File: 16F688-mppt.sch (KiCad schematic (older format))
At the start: 45 parts, among them Q1 BUK9511-55A127, Q2 BUK9511-55A127, Q3 2N2222A, Q4 2N2222A, Q5 2N2907A, SW1 Write OP-AMP DIFF, U1 7805, U2 LM358N, U3 PIC16F688

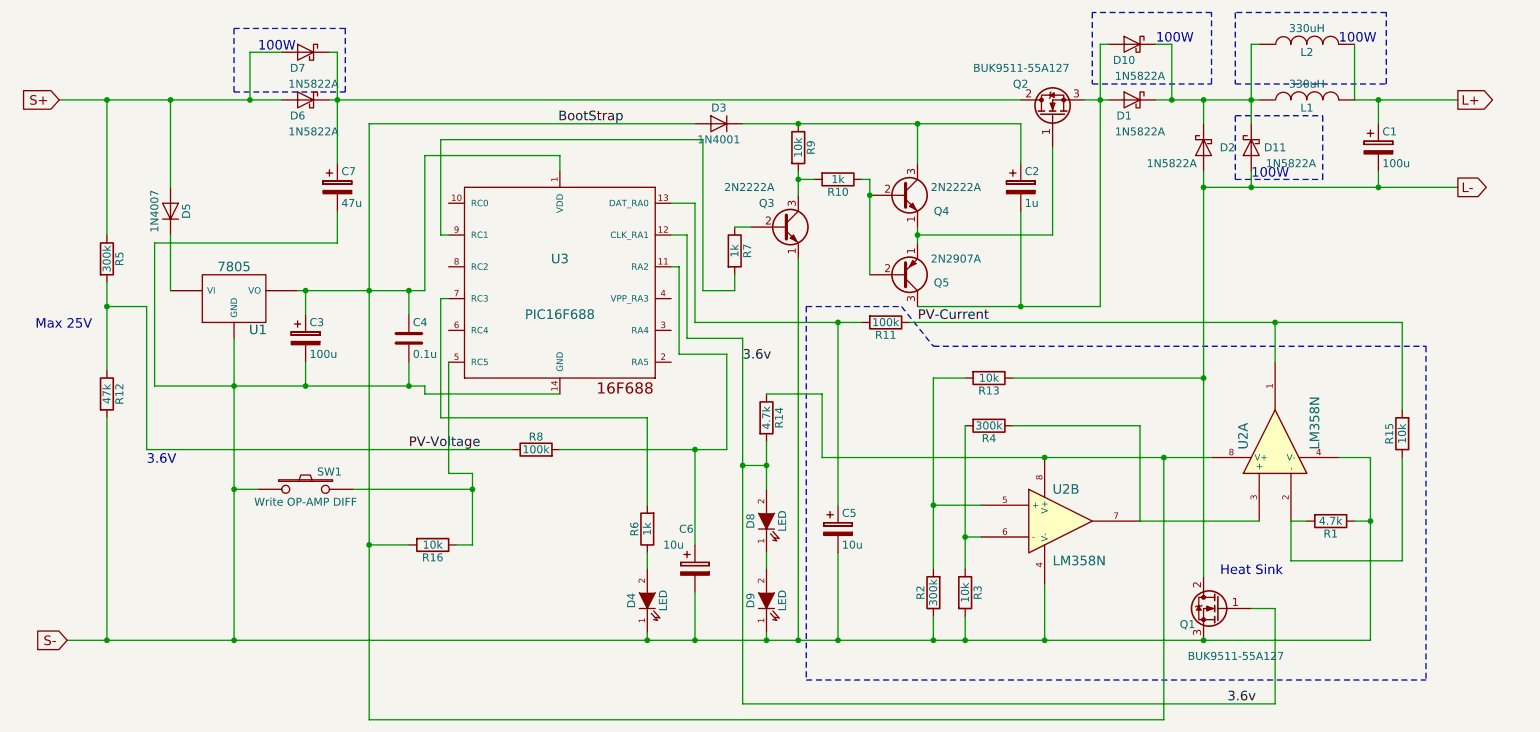
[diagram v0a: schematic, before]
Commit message: update schematic and code.
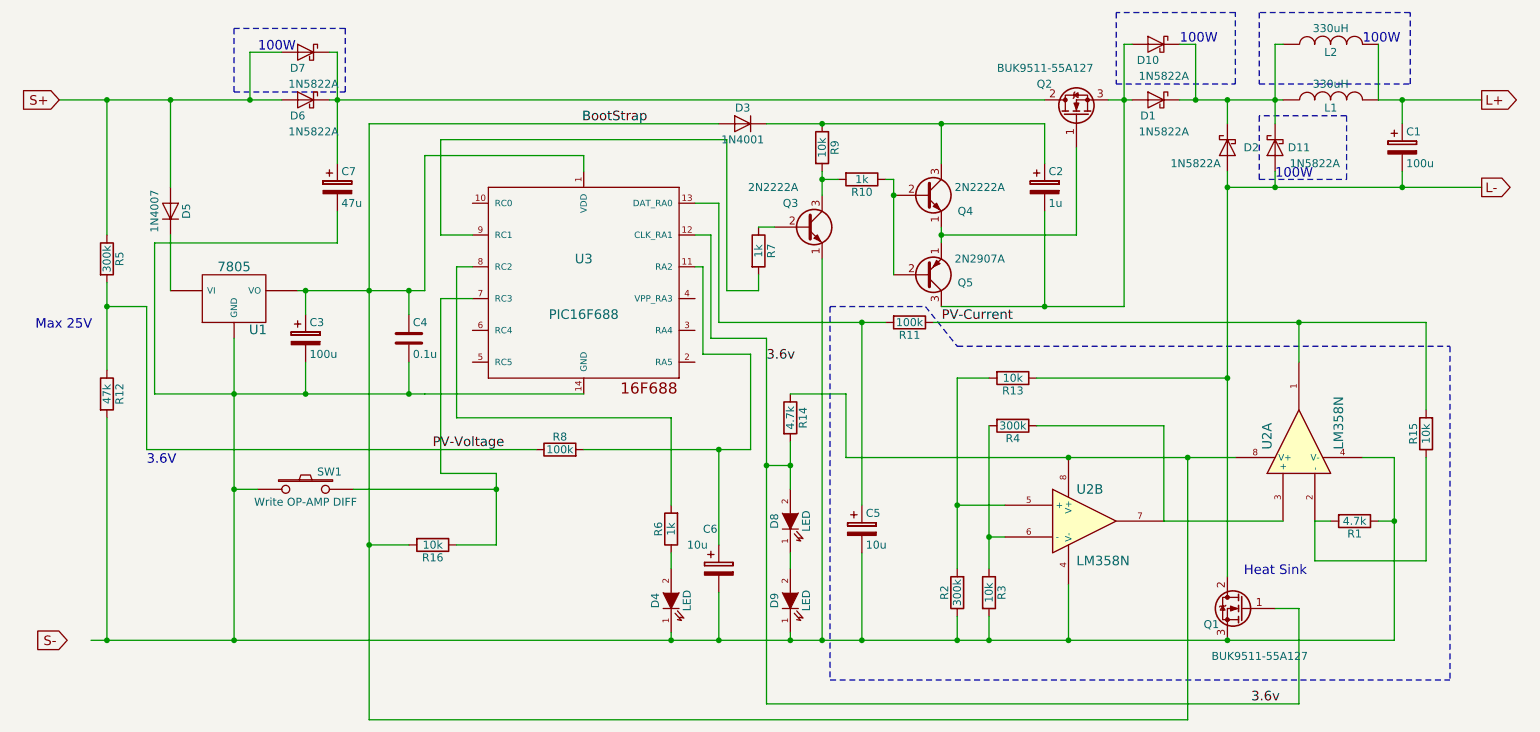
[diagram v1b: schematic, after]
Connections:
- net S-: no longer C3.2, C4.2, C5.2, C6.2, C7.2, D4.1 (K), D9.1 (K), Q1.3 (S), Q3.1 (E), R1.1, R12.2, R2.1, R3.2, SW1.1, U1.GND, U2.4 (V-), U2.4 (V-), U3.14 (GND)
- net at R6.2: now also U3.8 (RC2); no longer U3.7 (RC3)
- net at R16.1, SW1.2: now also U3.7 (RC3); no longer U3.5 (RC5)
- new net: C3.2, C4.2, C5.2, C6.2, C7.2, D4.1 (K), D9.1 (K), Q1.3 (S), Q3.1 (E), R1.1, R12.2, R2.1, R3.2, SW1.1, U1.GND, U2.4 (V-), U2.4 (V-), U3.14 (GND)
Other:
- moved on the sheet: C1, C2, C5, C6, D1, D10, D11, D2, D3, D4, D8, D9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

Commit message: More circuit simple.
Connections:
- net at R6.2: now also U3.6 (RC4); no longer U3.8 (RC2)
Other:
- moved on the sheet: D4, R6
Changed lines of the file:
@@
 Title "Simple MPPT with 16F688 v1"
 Date "2018-06-12"
-Rev "1.1"
+Rev "1.2"
 Comp ""
 Comment1 ""
@@
 L R R6
 U 1 1 55C3BCB8
-P 5050 4900
-F 0 "R6" V 5130 4900 50  0000 C CNN
-F 1 "1k" V 5050 4900 50  0000 C CNN
-F 2 "" V 4980 4900 30  0000 C CNN
-F 3 "" H 5050 4900 30  0000 C CNN
-	1    5050 4900
+P 4600 4800
+F 0 "R6" V 4680 4800 50  0000 C CNN
+F 1 "1k" V 4600 4800 50  0000 C CNN
+F 2 "" V 4530 4800 30  0000 C CNN
+F 3 "" H 4600 4800 30  0000 C CNN
+	1    4600 4800
 	-1   0    0    1
 $EndComp
@@
 L LED-RESCUE-12f675-mppt D4
 U 1 1 55C3BFD1
-P 5050 5350
-F 0 "D4" H 5050 5450 50  0000 C CNN
-F 1 "LED" H 5050 5250 50  0000 C CNN
-F 2 "" H 5050 5350 60  0000 C CNN
-F 3 "" H 5050 5350 60  0000 C CNN
-	1    5050 5350
+P 4600 5250
+F 0 "D4" H 4600 5350 50  0000 C CNN
+F 1 "LED" H 4600 5150 50  0000 C CNN
+F 2 "" H 4600 5250 60  0000 C CNN
+F 3 "" H 4600 5250 60  0000 C CNN
+	1    4600 5250
 	0    -1   -1   0
 $EndComp
@@
 	2750 4050 3400 4050
 Wire Wire Line
-	3400 4050 3500 4050
+	3400 4050 4500 4050
 Wire Wire Line
 	2300 3700 2300 4050
@@
 Connection ~ 1500 3500
 Wire Wire Line
-	5050 5600 5050 5550
-Connection ~ 5050 5600
-Wire Wire Line
-	5050 5150 5050 5050
+	4600 5600 4600 5450
+Connection ~ 4600 5600
+Wire Wire Line
+	4600 5050 4600 4950
 Wire Wire Line
 	1900 3050 1900 3400
@@
 	3150 6100 8300 6100
 Wire Wire Line
-	8300 6100 8300 4450
-Wire Wire Line
-	5050 4200 5050 4750
+	8300 4450 8300 6100
+Wire Wire Line
+	4600 4200 4600 4650
 Wire Wire Line
 	5350 5600 5350 5300
@@
 	5800 5600 5350 5600
 Wire Wire Line
-	5350 5600 5050 5600
-Wire Wire Line
-	5050 5600 2300 5600
+	5350 5600 4600 5600
+Wire Wire Line
+	4600 5600 2300 5600
 Wire Wire Line
 	2300 5600 1500 5600
@@
 Connection ~ 3150 5000
 Wire Wire Line
-	3950 5000 3950 4650
-Wire Wire Line
-	3950 4650 3950 4550
-Wire Wire Line
-	3700 5000 3950 5000
+	3950 4550 3950 4650
+Wire Wire Line
+	3950 4650 3950 5000
+Wire Wire Line
+	3950 5000 3700 5000
 Connection ~ 3950 4650
 Wire Wire Line
@@
 	4500 2550 4500 2650
 Wire Wire Line
-	3500 4050 3500 4050
-Wire Wire Line
-	3500 4050 4500 4050
-Wire Wire Line
 	3600 2450 5400 2450
 Wire Wire Line
 	5400 2450 5400 3400
 Wire Wire Line
-	3700 4200 5050 4200
+	3700 4200 4600 4200
 Wire Wire Line
 	5350 3600 5350 2850
@@
 	9300 2300 8750 2300
 Wire Wire Line
-	3700 3250 3800 3250
-Wire Wire Line
-	3700 3250 3700 4200
-Wire Wire Line
 	3600 4550 3600 3450
 Wire Wire Line
 	3600 3450 3800 3450
+Wire Wire Line
+	3800 3650 3700 3650
+Wire Wire Line
+	3700 3650 3700 4200
 $EndSCHEMATC

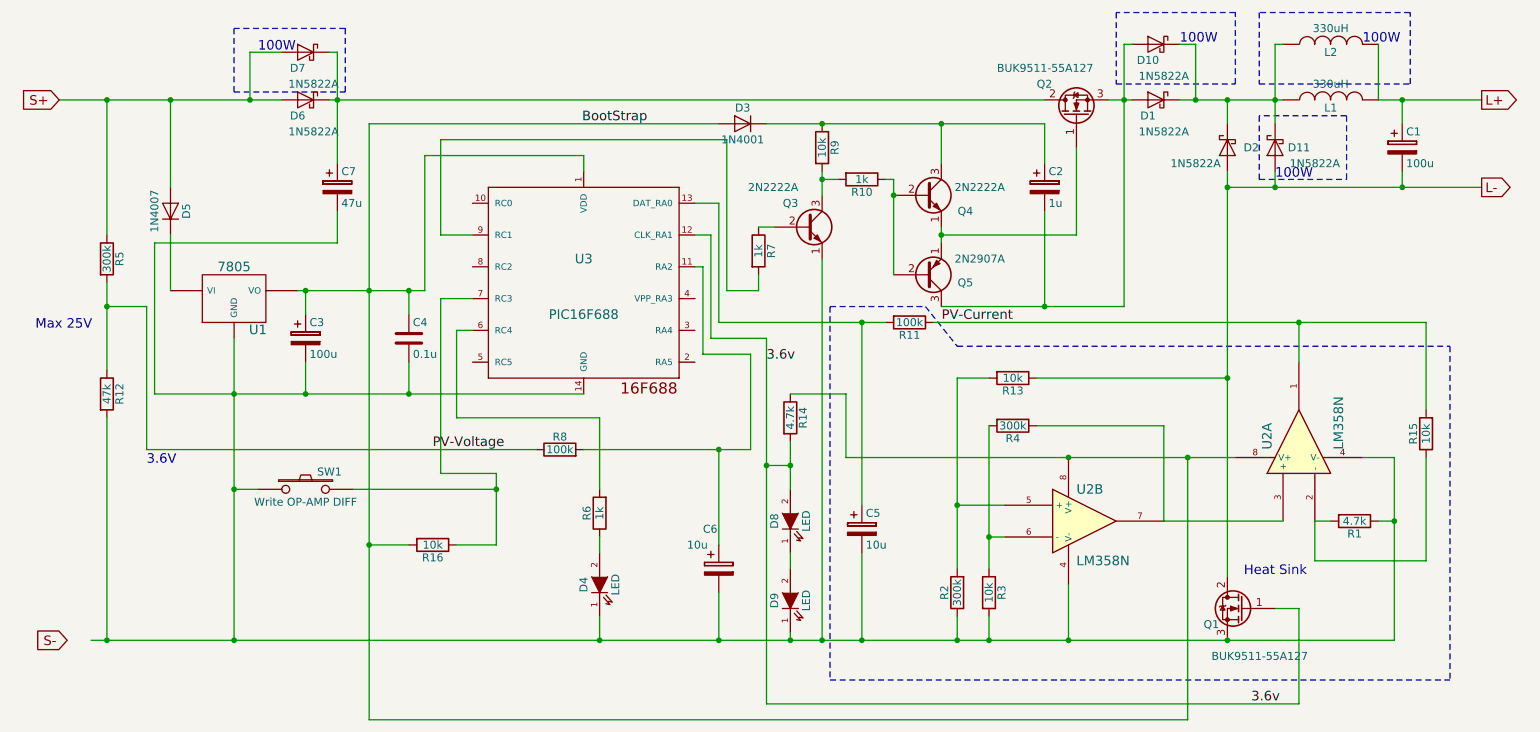
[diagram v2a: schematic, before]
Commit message: make word size and delay 300ms on op-amp calibration.
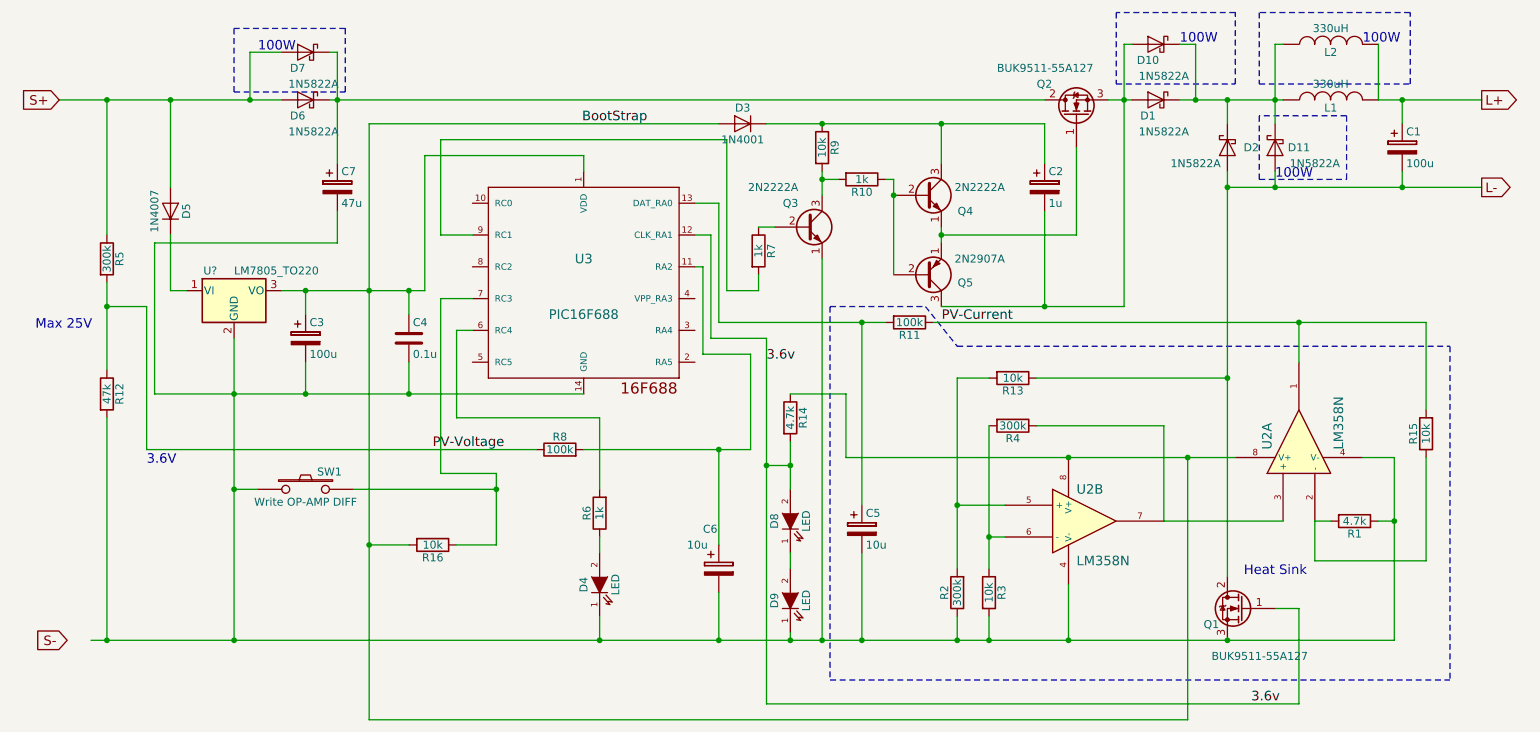
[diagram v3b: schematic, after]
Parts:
- removed U1: 7805, symbol 7805
- added U?: LM7805_TO220, TO_SOT_Packages_THT:TO-220_Vertical, symbol LM7805_TO220
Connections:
- net BootStrap: now also U?.3 (VO)
- net at C3.2, C4.2, C5.2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: now also U?.2 (GND)
- net at D5.1 (K): now also U?.1 (VI)
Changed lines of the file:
@@
 $EndDescr
-$Comp
-L 7805 U1
-U 1 1 55C337A7
-P 2300 3450
-F 0 "U1" H 2450 3254 60  0000 C CNN
-F 1 "7805" H 2300 3650 60  0000 C CNN
-F 2 "" H 2300 3450 60  0000 C CNN
-F 3 "" H 2300 3450 60  0000 C CNN
-	1    2300 3450
-	1    0    0    -1
-$EndComp
 $Comp
 L Q_NMOS_GDS Q1
@@
 100W
 Wire Wire Line
-	1800 4050 2300 4050
-Wire Wire Line
-	2300 4050 2750 4050
-Wire Wire Line
-	2750 4050 3400 4050
-Wire Wire Line
-	3400 4050 4500 4050
-Wire Wire Line
-	2300 3700 2300 4050
-Wire Wire Line
-	2300 4050 2300 4650
-Wire Wire Line
-	2300 4650 2300 5600
+	1800 4050 4500 4050
+Wire Wire Line
+	2300 3700 2300 5600
 Connection ~ 2300 4050
 Wire Wire Line
-	2700 3400 2750 3400
-Wire Wire Line
-	2750 3400 3150 3400
-Wire Wire Line
-	3150 3400 3400 3400
-Wire Wire Line
-	3400 3400 3500 3400
+	2600 3400 3500 3400
 Wire Wire Line
 	7550 5600 7550 5250
 Wire Wire Line
-	3150 2350 3150 3400
-Wire Wire Line
-	3150 3400 3150 5000
-Wire Wire Line
-	3150 5000 3150 6100
+	3150 2350 3150 6100
 Connection ~ 3150 3400
 Wire Wire Line
@@
 	7150 4950 7050 4950
 Wire Wire Line
-	7050 4250 7050 4950
-Wire Wire Line
-	7050 4950 7050 5150
+	7050 4250 7050 5150
 Connection ~ 7050 4950
 Wire Wire Line
 	6850 4750 7150 4750
 Wire Wire Line
-	8550 2650 8550 2750
-Wire Wire Line
-	8550 2750 8550 3950
-Wire Wire Line
-	8550 3950 8550 5200
-Wire Wire Line
-	8550 2750 8850 2750
-Wire Wire Line
-	8850 2750 9650 2750
-Wire Wire Line
-	9650 2750 10150 2750
-Wire Wire Line
-	8250 2200 8350 2200
-Wire Wire Line
-	8350 2200 8550 2200
-Wire Wire Line
-	8550 2200 8850 2200
-Wire Wire Line
-	8850 2200 8900 2200
+	8550 2650 8550 5200
+Wire Wire Line
+	8550 2750 10150 2750
+Wire Wire Line
+	8250 2200 8900 2200
 Wire Wire Line
 	8550 2200 8550 2350
 Connection ~ 8550 2200
 Wire Wire Line
-	9500 2200 9650 2200
-Wire Wire Line
-	9650 2200 10150 2200
+	9500 2200 10150 2200
 Wire Wire Line
 	9650 2200 9650 2350
 Wire Wire Line
-	7800 2200 7900 2200
-Wire Wire Line
-	7900 2200 7950 2200
-Wire Wire Line
-	6750 3000 6750 3050
-Wire Wire Line
-	6750 3050 6750 3100
+	7800 2200 7950 2200
+Wire Wire Line
+	6750 3000 6750 3100
 Wire Wire Line
 	6750 3050 7600 3050
@@
 Connection ~ 6750 3050
 Wire Wire Line
-	7900 3500 7400 3500
-Wire Wire Line
-	7400 3500 6750 3500
-Wire Wire Line
-	7900 1850 7900 2200
-Wire Wire Line
-	7900 2200 7900 3500
+	7900 3500 6750 3500
+Wire Wire Line
+	7900 1850 7900 3500
 Connection ~ 7900 2200
 Wire Wire Line
-	6450 2700 6450 2800
-Wire Wire Line
-	6450 2800 6450 3300
+	6450 2700 6450 3300
 Wire Wire Line
 	7400 2900 7400 3500
@@
 Connection ~ 6000 5600
 Wire Wire Line
-	6000 2650 6000 2700
-Wire Wire Line
-	6000 2700 6000 2800
+	6000 2650 6000 2800
 Wire Wire Line
 	5400 3400 5600 3400
@@
 	5600 3000 5700 3000
 Wire Wire Line
-	5650 2350 6000 2350
-Wire Wire Line
-	6000 2350 6750 2350
-Wire Wire Line
-	6750 2350 7400 2350
+	5650 2350 7400 2350
 Wire Wire Line
 	6750 2350 6750 2600
@@
 	1500 3050 1500 2200
 Wire Wire Line
-	1500 3350 1500 3500
-Wire Wire Line
-	1500 3500 1500 3900
+	1500 3350 1500 3900
 Wire Wire Line
 	1750 3500 1500 3500
@@
 	6050 5850 9950 5850
 Wire Wire Line
-	5350 3600 6250 3600
-Wire Wire Line
-	6250 3600 6400 3600
+	5350 3600 6400 3600
 Wire Wire Line
 	1500 4200 1500 5600
 Connection ~ 1500 5600
 Wire Wire Line
-	6850 3950 6850 4750
-Wire Wire Line
-	6850 4750 6850 5150
+	6850 3950 6850 5150
 Wire Wire Line
 	6850 5600 6850 5450
@@
 Connection ~ 8550 3950
 Wire Wire Line
-	5800 4350 5800 4500
-Wire Wire Line
-	5800 4500 5800 4650
+	5800 4350 5800 4650
 Wire Wire Line
 	5800 5050 5800 5150
@@
 	3150 6100 8300 6100
 Wire Wire Line
-	8300 4450 8300 6100
+	8300 6100 8300 4450
 Wire Wire Line
 	4600 4200 4600 4650
@@
 	1750 4400 4200 4400
 Wire Wire Line
-	4500 4400 5350 4400
-Wire Wire Line
-	5350 4400 5550 4400
+	4500 4400 5550 4400
 Wire Wire Line
 	5550 4400 5550 3800
@@
 	5800 4500 5650 4500
 Wire Wire Line
-	5650 3700 5650 4500
-Wire Wire Line
-	5650 4500 5650 6000
+	5650 3700 5650 6000
 Connection ~ 5800 4500
 Wire Wire Line
@@
 Connection ~ 5650 4500
 Wire Wire Line
-	6150 4450 7550 4450
-Wire Wire Line
-	7550 4450 8300 4450
-Wire Wire Line
-	8300 4450 8600 4450
-Wire Wire Line
-	9600 5600 8550 5600
-Wire Wire Line
-	8550 5600 7550 5600
-Wire Wire Line
-	7550 5600 7050 5600
-Wire Wire Line
-	7050 5600 6850 5600
-Wire Wire Line
-	6850 5600 6250 5600
-Wire Wire Line
-	6250 5600 6000 5600
-Wire Wire Line
-	6000 5600 5800 5600
-Wire Wire Line
-	5800 5600 5350 5600
-Wire Wire Line
-	5350 5600 4600 5600
-Wire Wire Line
-	4600 5600 2300 5600
-Wire Wire Line
-	2300 5600 1500 5600
-Wire Wire Line
-	1500 5600 1400 5600
+	6150 4450 8600 4450
+Wire Wire Line
+	9600 5600 1400 5600
 Wire Wire Line
 	8150 4250 8150 4850
@@
 	9000 3850 9000 3600
 Wire Wire Line
-	6700 3600 9000 3600
-Wire Wire Line
-	9000 3600 9800 3600
-Wire Wire Line
-	9600 4450 9600 4850
-Wire Wire Line
-	9600 4850 9600 5600
+	6700 3600 9800 3600
+Wire Wire Line
+	9600 4450 9600 5600
 Connection ~ 8550 5600
 Wire Wire Line
@@
 	9100 5100 9100 4850
 Wire Wire Line
-	1200 2200 1500 2200
-Wire Wire Line
-	1500 2200 1900 2200
-Wire Wire Line
-	1900 2200 2400 2200
-Wire Wire Line
-	2400 2200 2600 2200
-Wire Wire Line
-	2900 2200 2950 2200
-Wire Wire Line
-	2950 2200 7400 2200
-Wire Wire Line
-	2950 1900 2950 2200
-Wire Wire Line
-	2950 2200 2950 2600
+	1200 2200 2600 2200
+Wire Wire Line
+	2900 2200 7400 2200
+Wire Wire Line
+	2950 1900 2950 2600
 Connection ~ 2950 2200
 Wire Wire Line
@@
 Connection ~ 3150 5000
 Wire Wire Line
-	3950 4550 3950 4650
-Wire Wire Line
-	3950 4650 3950 5000
+	3950 4550 3950 5000
 Wire Wire Line
 	3950 5000 3700 5000
@@
 Connection ~ 8850 2750
 Wire Wire Line
-	8850 1850 8850 2200
-Wire Wire Line
-	8850 2200 8850 2350
+	8850 1850 8850 2350
 Connection ~ 8850 2200
 Wire Wire Line
@@
 Wire Wire Line
 	3700 3650 3700 4200
+$Comp
+L LM7805_TO220 U?
+U 1 1 5B23C839
+P 2300 3400
+F 0 "U?" H 2150 3525 50  0000 C CNN
+F 1 "LM7805_TO220" H 2300 3525 50  0000 L CNN
+F 2 "TO_SOT_Packages_THT:TO-220_Vertical" H 2300 3625 50  0001 C CIN
+F 3 "" H 2300 3350 50  0001 C CNN
+	1    2300 3400
+	1    0    0    -1
+$EndComp
+Wire Wire Line
+	1900 3400 2000 3400
 $EndSCHEMATC

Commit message: Remove R11.
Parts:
- removed R11: 100k, symbol R
- C1, C2, C3, C5, C6, C7: symbol CP -> Device:CP
- C4: symbol C -> Device:C
- D1, D10, D11, D2, D6, D7: symbol D_Schottky -> Device:D_Schottky
- D3: value 1N4001 -> 1N4148; symbol D -> Device:D
- D4, D8, D9: symbol LED-RESCUE-12f675-mppt -> 16F688-mppt-rescue:LED-RESCUE-12f675-mppt
- D5: symbol D -> Device:D
- L1, L2: symbol INDUCTOR -> 16F688-mppt-rescue:INDUCTOR
- Q1, Q2: symbol Q_NMOS_GDS -> Device:Q_NMOS_GDS
- Q3, Q4: symbol Q_NPN_EBC -> Device:Q_NPN_EBC
- Q5: symbol Q_PNP_EBC -> Device:Q_PNP_EBC
- R1, R10, R12, R13, R14, R15, R16, R2, R3, R4, R5, R6, R7, R8, R9: symbol R -> Device:R
- SW1: symbol SW_PUSH -> 16F688-mppt-rescue:SW_PUSH
- U1: renamed from U?; symbol LM7805_TO220 -> 16F688-mppt-rescue:LM7805_TO220
- U2: symbol LM358N-RESCUE-12f675-mppt -> 16F688-mppt-rescue:LM358N-RESCUE-12f675-mppt
- U3: symbol PIC16F688 -> microchip-16f688:PIC16F688
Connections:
- net PV-Current: now also C5.1, U3.13 (DAT_RA0)
